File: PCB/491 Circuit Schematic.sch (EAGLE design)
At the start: 29 parts, among them IC1 7812T, X1 B4B-ZR

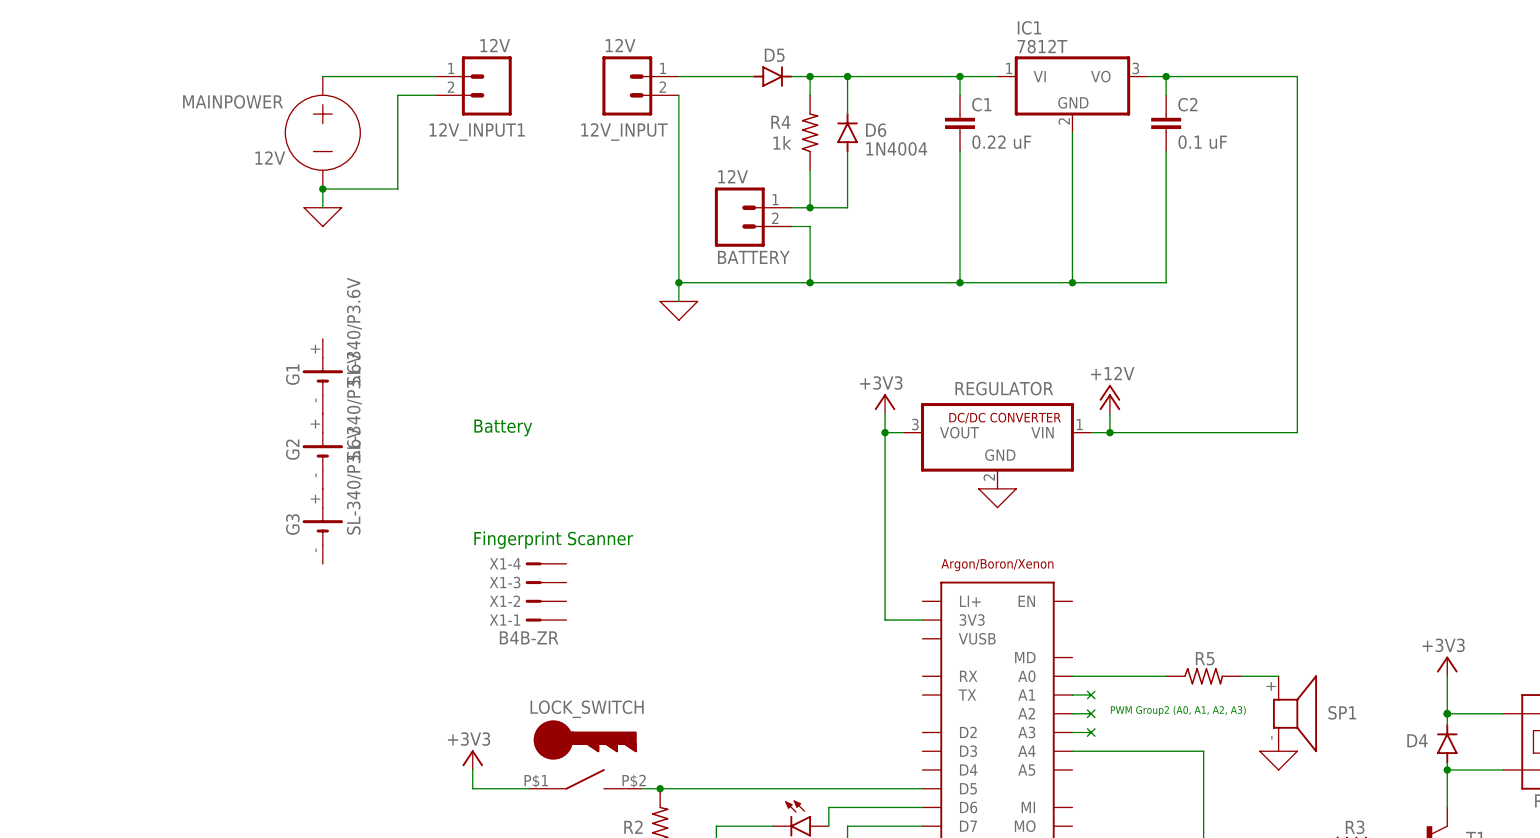
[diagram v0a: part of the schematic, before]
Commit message: PCB Update
Added FPS and Voltage Regulator.
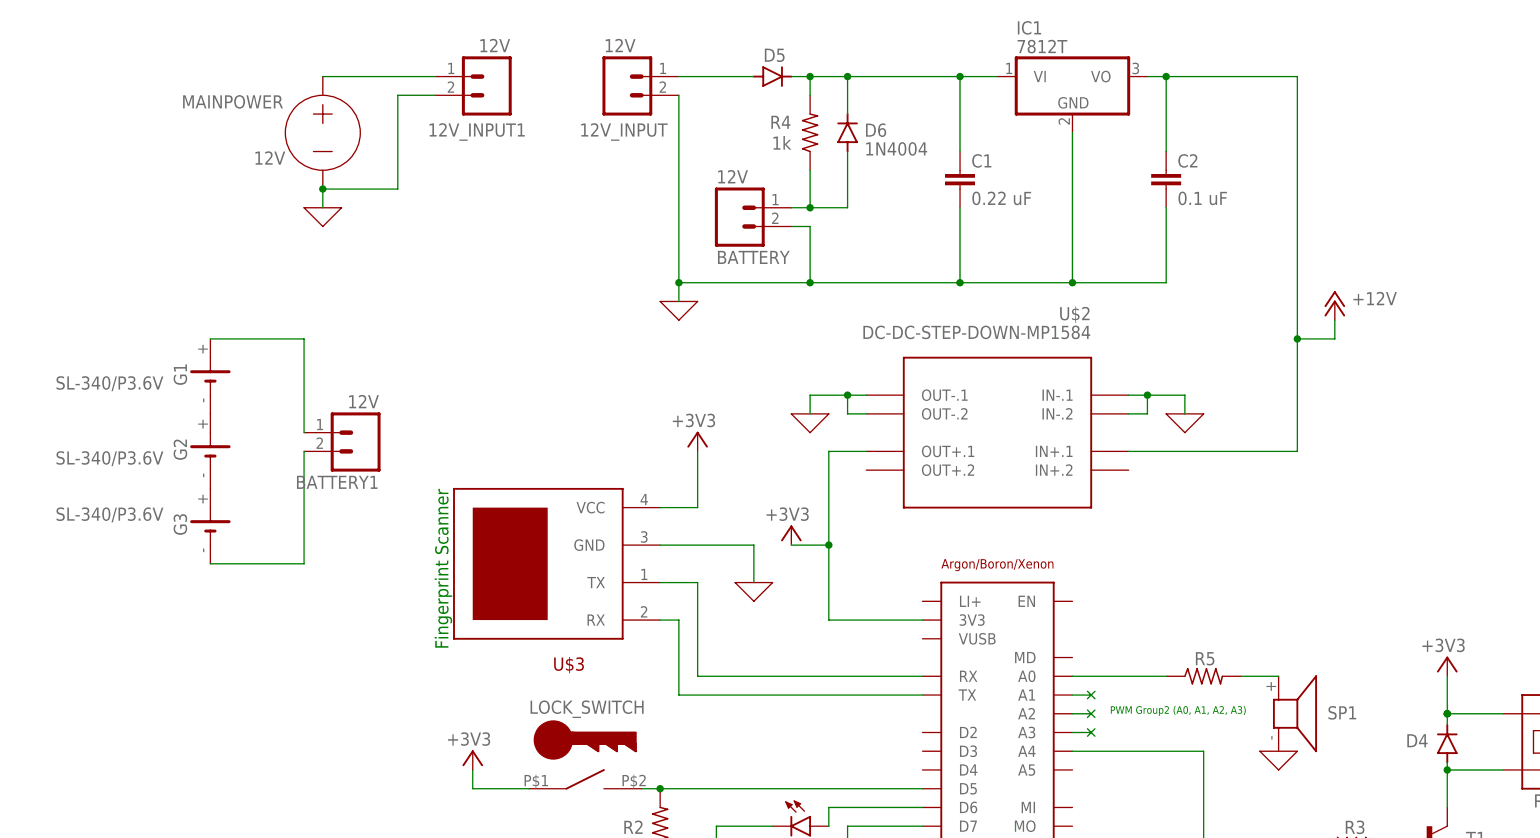
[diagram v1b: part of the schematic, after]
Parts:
- removed REGULATOR: R-78C1.8-1.0, dc-dc-converter:R-78C1.8-1.0
- removed X1: B4B-ZR, con-jst:B4B-ZR
- added BATTERY1: 12V, con-amp-quick:M02
- added U$2: DC-DC-STEP-DOWN-MP1584, cool_safe_lib:DC-DC-STEP-DOWN-MP1584
- added U$3: FPS, cool_safe_lib:FPS
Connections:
- new net N$16: U$1.RX, U$3.TX
- new net N$28: U$1.TX, U$3.RX
- new net N$30: BATTERY1.1, G1.+
- new net N$31: BATTERY1.2, G3.-
- net +12V: now also U$2.IN+.1; no longer REGULATOR.VIN
- net +3V3: now also U$2.OUT+.1, U$3.VCC; no longer REGULATOR.VOUT
- net 0: now also U$2.IN-.1, U$2.IN-.2, U$2.OUT-.1, U$2.OUT-.2, U$3.GND
- net FPS: no longer REGULATOR.GND
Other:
- note removed: "Battery"
- moved on the sheet: C1, C2, G1, G2, G3

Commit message: PCB V1
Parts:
- removed 12V_INPUT, 12V_INPUT1, BATTERY1: 12V, con-amp-quick:M02
- removed G1, G2, G3: SL-340/P3.6V, battery:SL-340/P3.6V
- removed IC1: 7812T, linear:7812T
- removed MAINPOWER: 12V, ngspice-simulation:VOLTAGE
- added 12V_EXT, 12V_IN, BATTERY_EXT: 12V, con-amp-quick:M02
- added B1, B2, B3: SL-340/P3.6V, battery:SL-340/P3.6V
- added FRIDGE_POWER: 12V, ngspice-simulation:VOLTAGE
- C1: value 0.22 uF -> 47 uF; device capacitor-wima:C2.5/5 -> rcl:CPOL-USE2.5-6
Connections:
- removed net N$15: C1.1, D5.C, D6.C, IC1.VI, R4.2
- removed net N$31: BATTERY1.2, G3.-
- net +12V: now also C1.+, D5.C, D6.C, R4.2; no longer IC1.VO
- net 0: now also 12V_EXT.2, 12V_IN.2, B1.-, BATTERY_EXT.2, C1.-, FRIDGE_POWER.-; no longer 12V_INPUT.2, 12V_INPUT1.2, C1.2, IC1.GND, MAINPOWER.-
- net N$1: now also 12V_EXT.1, FRIDGE_POWER.+; no longer 12V_INPUT1.1, MAINPOWER.+
- net N$29: now also 12V_IN.1; no longer 12V_INPUT.1
- net N$3: now also B2.+, B3.-; no longer G1.-, G2.+
- net N$30: now also B3.+, BATTERY_EXT.1; no longer BATTERY1.1, G1.+
- net N$5: now also B1.+, B2.-; no longer G2.-, G3.+
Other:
- note added: "1.0"
- note added: "3S Li-ion Battery Pack (11.1V)"
- note added: "Cool Safe"
- moved on the sheet: BATTERY, C2, D1, D2, D3, D4, D5, D6, LOCK_SWITCH, R1, R2, R3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

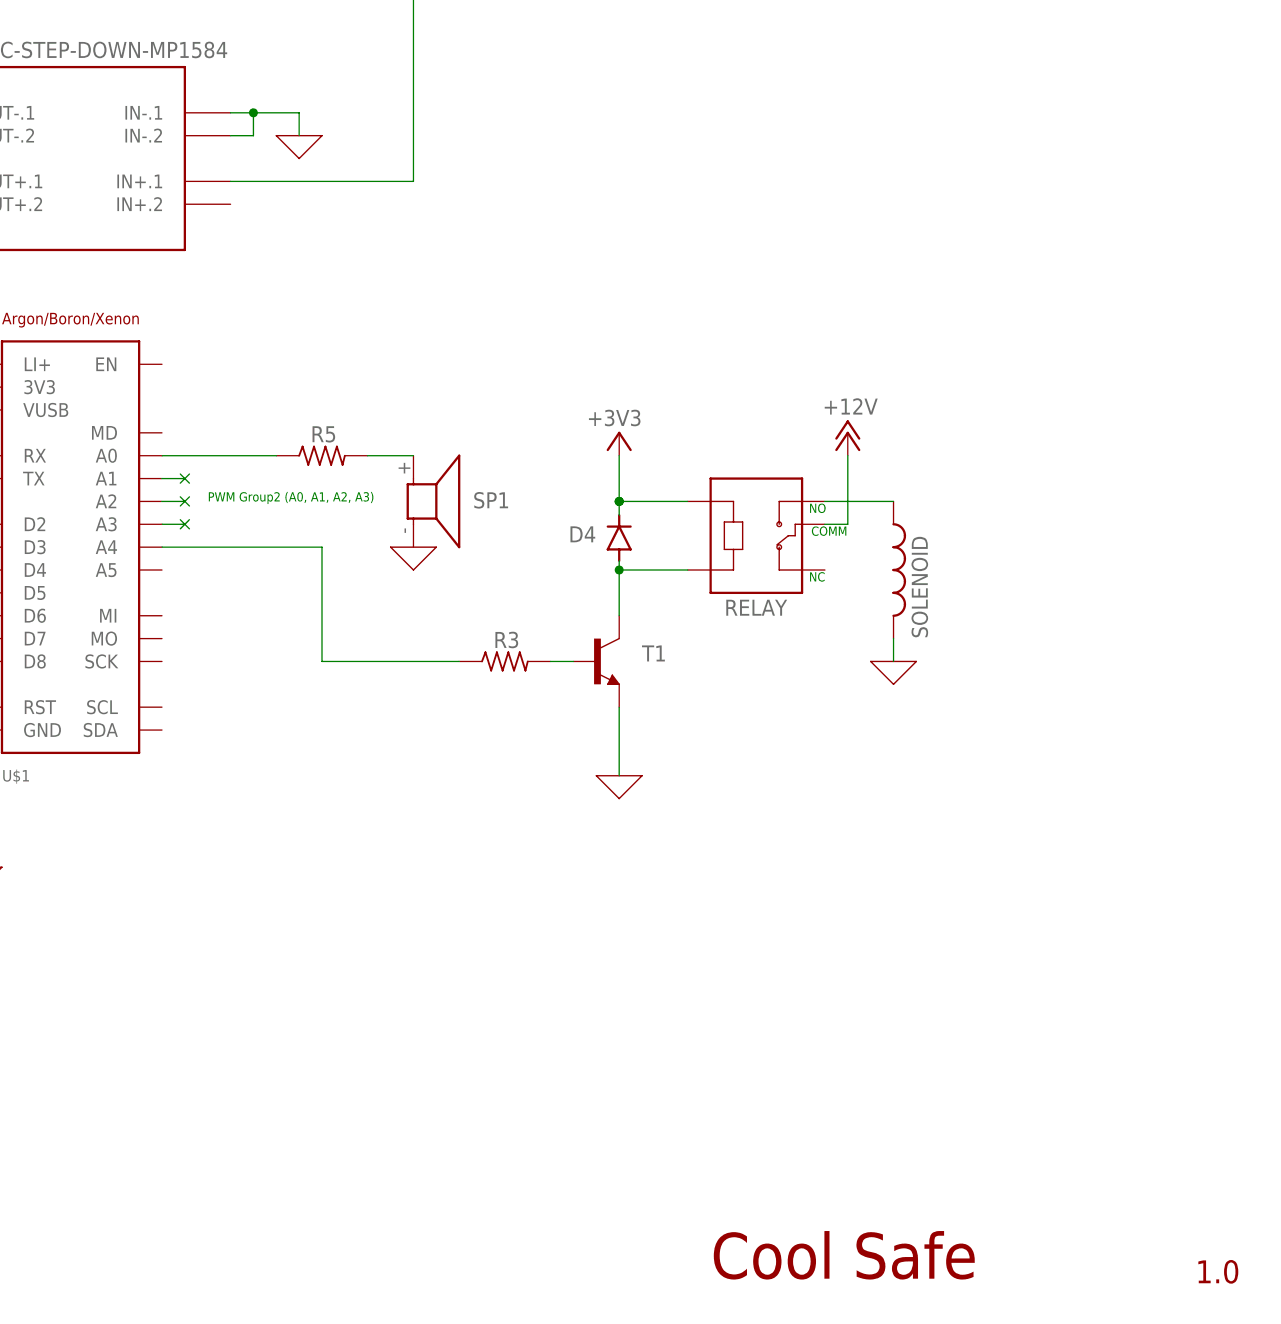
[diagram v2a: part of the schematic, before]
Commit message: Edited Schematic, started layout
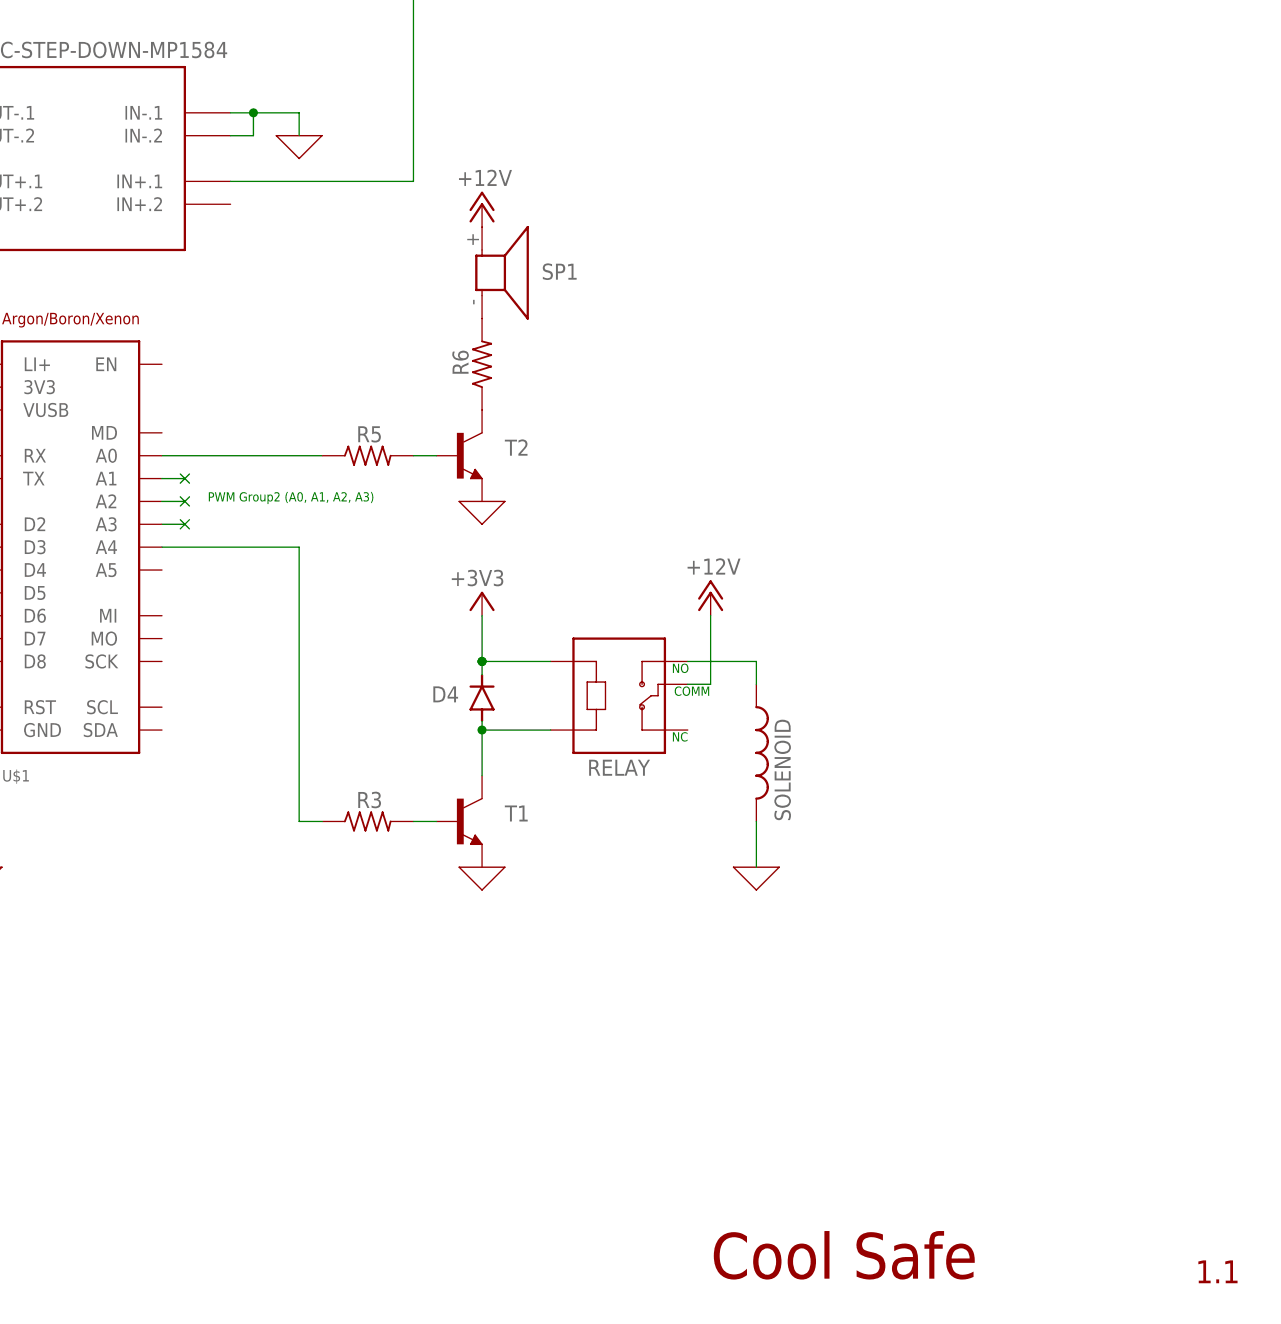
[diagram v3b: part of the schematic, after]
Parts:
- added R6: (no value), rcl:R-US_0204/7
- added T2: (no value), transistor:-NPN-TO92
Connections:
- removed net FPS: SP1.2
- new net N$15: R6.1, T2.C
- new net N$31: R6.2, SP1.2
- net +12V: now also SP1.1
- net 0: now also T2.E
- net N$2: now also T2.B; no longer SP1.1
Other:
- note added: "1.1"
- note removed: "1.0"
- moved on the sheet: D4, R3, R5, RELAY, SP1, T1
